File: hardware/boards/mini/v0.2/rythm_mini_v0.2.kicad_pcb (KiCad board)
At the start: 8 copper layers, 20 x 41 mm, 102 parts, among them IC1 NAU88C22YG, IC3 IS42S16160J-6BLI, J2 Top, J3 Bottom, Q1 PMV37EN22, U1 W25Q128JVP, U2 LTV-217-G, U4 STM32H750XBHx, Y1 Crystal_GND24

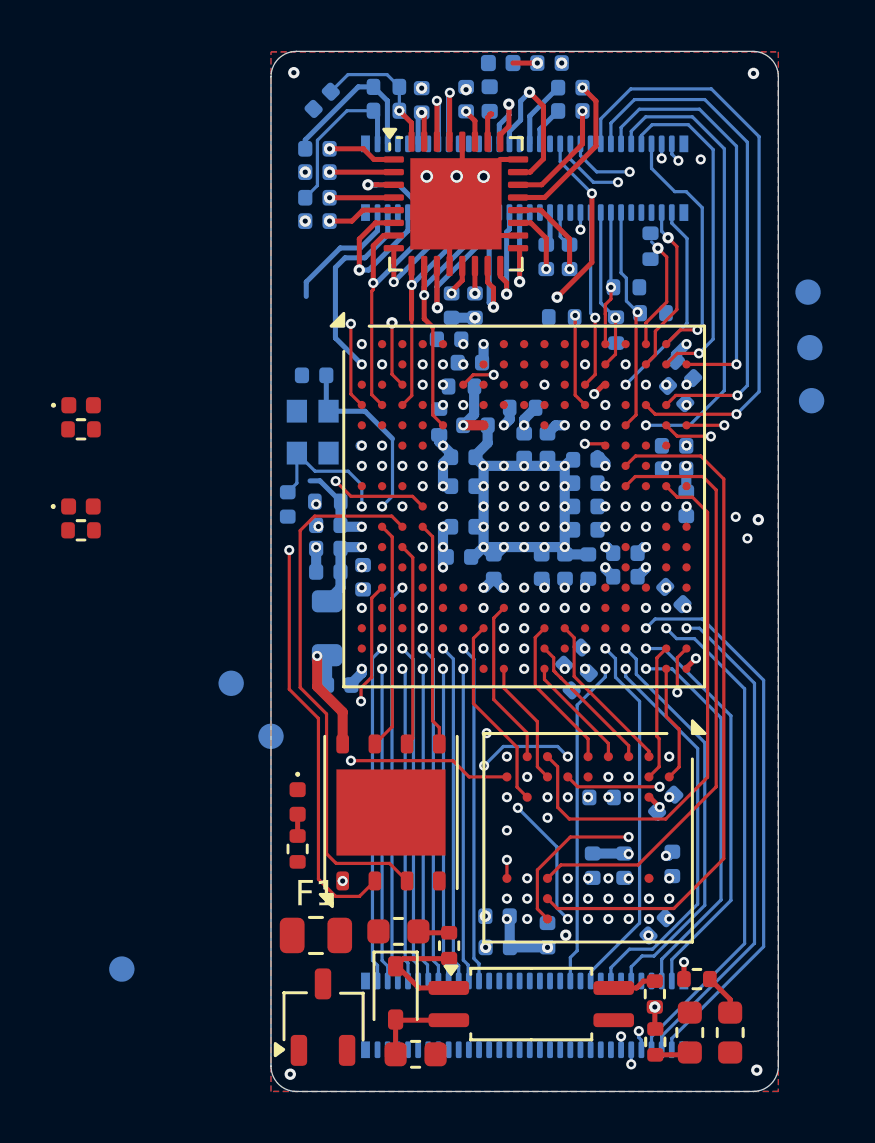
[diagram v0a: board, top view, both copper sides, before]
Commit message: mini: remove unused test points
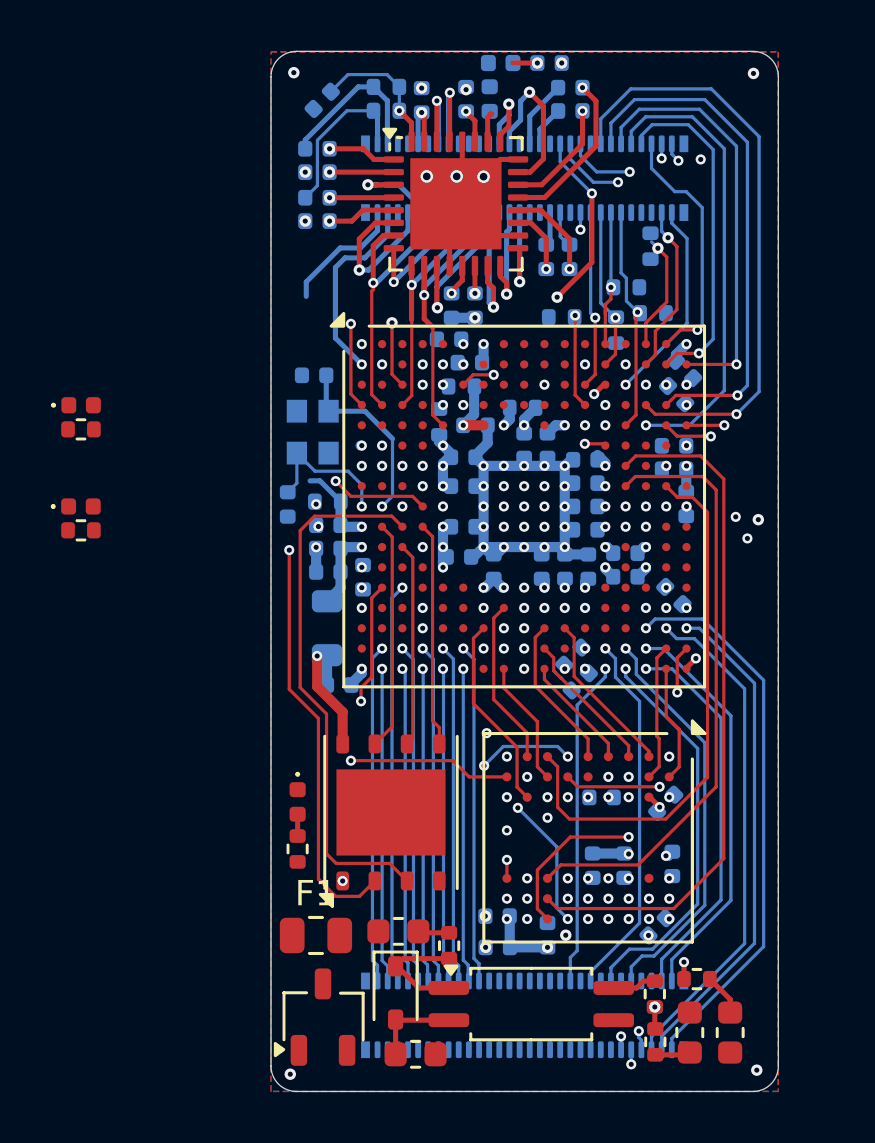
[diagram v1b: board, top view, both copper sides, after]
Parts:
- removed TP1: GND, TestPoint:TestPoint_Pad_D1.0mm
- removed TP2: VIN, TestPoint:TestPoint_Pad_D1.0mm
- removed TP3: 3v3, TestPoint:TestPoint_Pad_D1.0mm
- removed TP4: SWD_IO, TestPoint:TestPoint_Pad_D1.0mm
- removed TP5: SWD_CLK, TestPoint:TestPoint_Pad_D1.0mm
- removed TP6: SWD_SWO, TestPoint:TestPoint_Pad_D1.0mm

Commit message: mini: start routing QSPI to lower connector
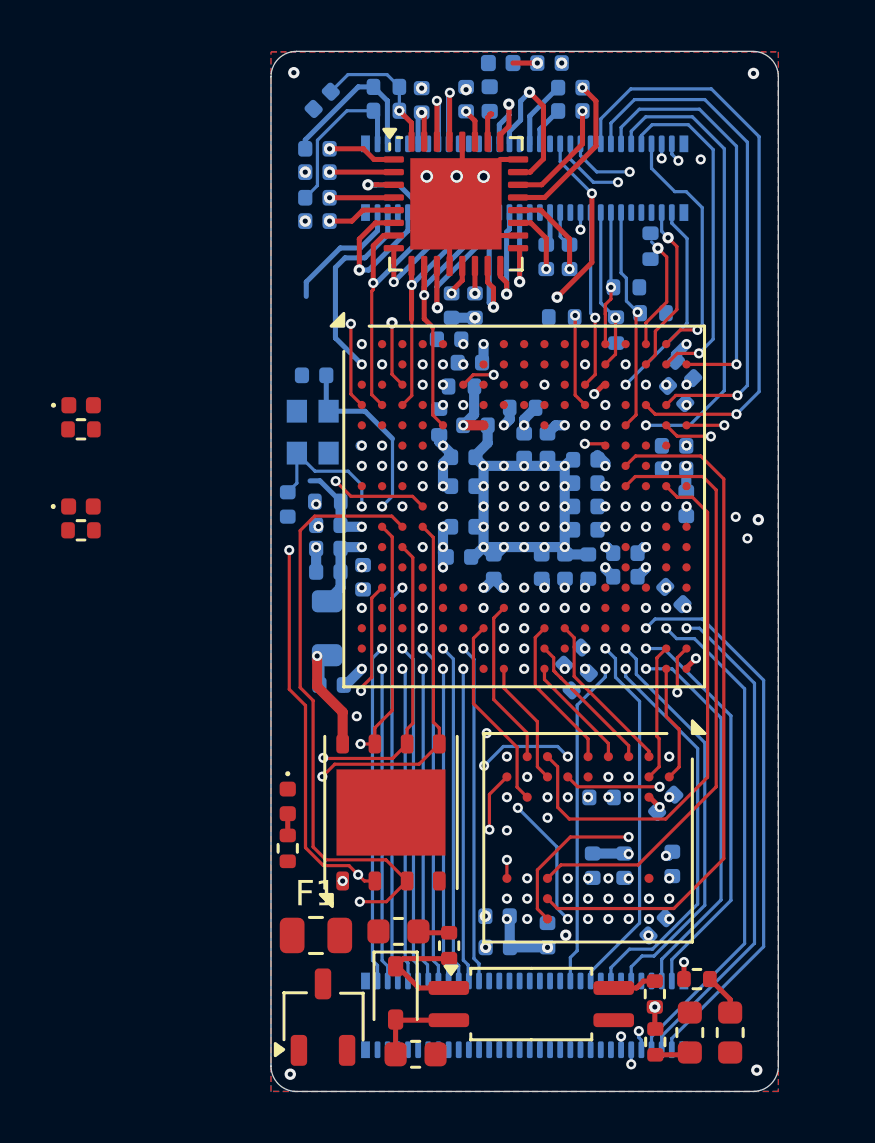
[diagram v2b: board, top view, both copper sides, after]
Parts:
- moved D1 0.39 mm to (70.7, 86.6)
- moved R16 0.39 mm to (70.7, 88.4)
- moved C32 0.30 mm to (72.4, 82.0)
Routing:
- net /QSPI_IO0: track 8.83 -> 15.2 mm, vias 0 -> 1
- net /QSPI_CLK: track 8.03 -> 12.9 mm, vias 0 -> 1
- net /QSPI_IO3: track 9.01 -> 12.6 mm, vias 0 -> 1
- net /QSPI_IO2: track 21.2 -> 24.4 mm, vias 0 -> 1
- net /FMC_A5: track 21.5 -> 23.0 mm, vias 2 -> 3
- net /QSPI_IO1: track 21.9 -> 22.6 mm, vias 2 -> 3
- net /FMC_A3: track 17.8 -> 18.5 mm
- net /FMC_A1: track 20.1 -> 20.6 mm

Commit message: mini: route external QSPI lines and LEDs
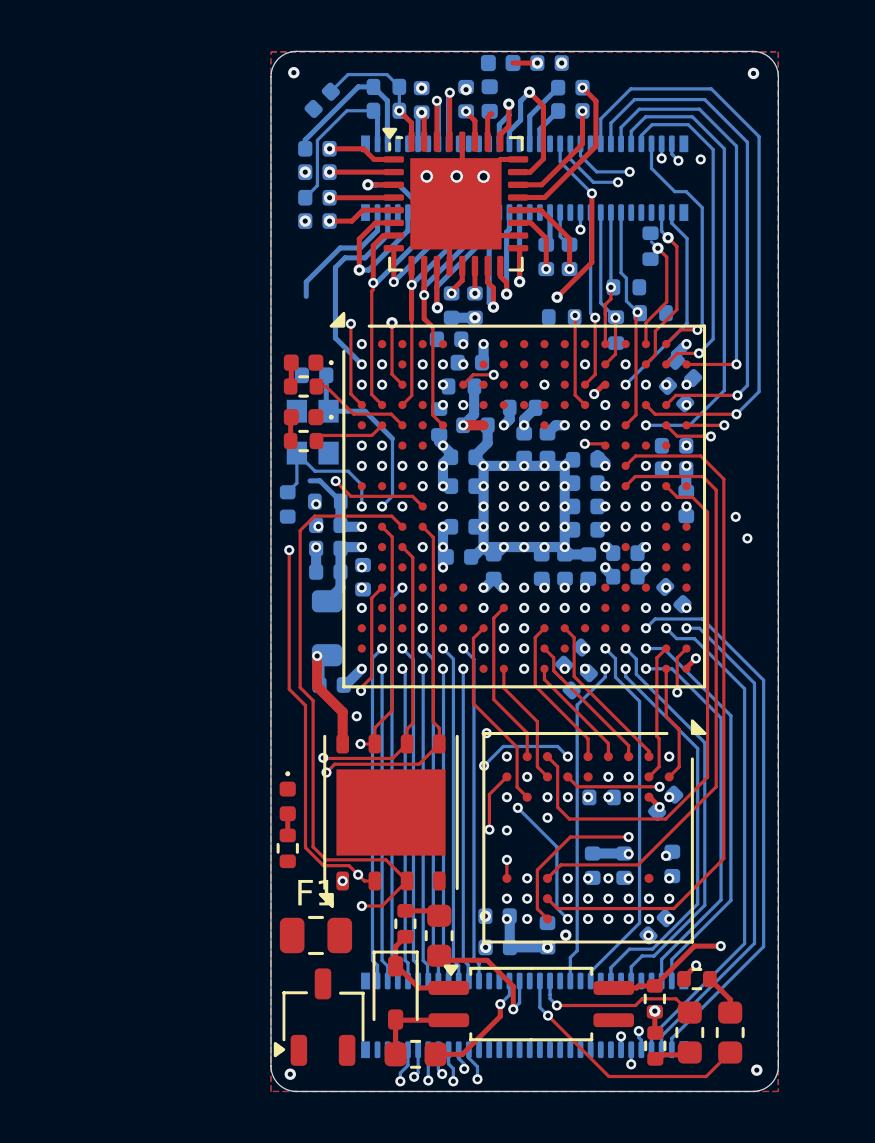
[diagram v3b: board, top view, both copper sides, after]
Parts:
- moved D4 9.46 mm to (71.3, 71.4), turned to 180 degrees
- moved R17 9.45 mm to (71.3, 72.4), turned to 180 degrees
- moved R15 8.94 mm to (71.3, 70.2), turned to 180 degrees
- moved D2 8.93 mm to (71.3, 69.3), turned to 180 degrees
- moved R7 1.93 mm to (75.3, 91.4)
- moved FB2 1.62 mm to (76.6, 91.9), turned to 90 degrees
- moved R6 0.19 mm to (85.1, 94.3)
- moved R9 0.16 mm to (85.2, 96.2)
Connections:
- J3 pad 25: /DIN_OUT_SINK -> /DIN_OUT_SOURCE
- J3 pad 27: /DIN_OUT_SOURCE -> /DIN_OUT_SINK
- J3 pad 42: unconnected-(J3-Pad42) -> /EXT_QSPI_DETECT
- J3 pad 44: unconnected-(J3-Pad44) -> /QSPI_CS_EXP
- J3 pad 46: unconnected-(J3-Pad46) -> /QSPI_IO3
- J3 pad 48: unconnected-(J3-Pad48) -> /QSPI_IO2
- J3 pad 50: unconnected-(J3-Pad50) -> /QSPI_IO1
- J3 pad 52: unconnected-(J3-Pad52) -> /QSPI_IO0
- J3 pad 54: unconnected-(J3-Pad54) -> /QSPI_CLK
- U4 pad E2: unconnected-(U4I-PI9-PadE2) -> /LED_STATUS2
- U4 pad E3: unconnected-(U4C-PC13-PadE3) -> /LED_STATUS
- U4 pad F14: /LED_STATUS -> unconnected-(U4C-PC6-PadF14)
- U4 pad G15: unconnected-(U4G-PG6-PadG15) -> /QSPI_CS_EXP
- U4 pad H15: unconnected-(U4G-PG3-PadH15) -> /EXT_QSPI_DETECT
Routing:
- net /EXT_QSPI_DETECT: track 0.00 -> 38.4 mm, vias 0 -> 2
- net /QSPI_CS_EXP: track 0.00 -> 38.3 mm, vias 0 -> 2
- net /QSPI_CLK: track 12.9 -> 27.2 mm, vias 1 -> 2
- net /QSPI_IO3: track 12.6 -> 25.8 mm, vias 1 -> 2
- net /QSPI_IO0: track 15.2 -> 28.3 mm, vias 1 -> 2
- net /DIN_OUT_SINK: track 0.00 -> 10.1 mm, vias 0 -> 1
- net /QSPI_IO1: track 22.6 -> 31.5 mm, vias 3 -> 4
- net /QSPI_IO2: track 24.4 -> 32.5 mm, vias 1 -> 2
- net /DIN_OUT_SOURCE: track 0.00 -> 6.65 mm, vias 0 -> 1
- net /DIN_IN_SOURCE: track 0.00 -> 5.54 mm, vias 0 -> 1
- net /DIN_IN_SINK: track 0.00 -> 4.72 mm, vias 0 -> 1
- net /LED_STATUS: track 0.00 -> 4.02 mm
- net /LED_STATUS2: track 0.00 -> 2.84 mm
- net Net-(D2-A): track 0.00 -> 0.95 mm
- net Net-(D4-A): track 0.00 -> 0.95 mm
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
